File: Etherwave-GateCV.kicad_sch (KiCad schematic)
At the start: 57 parts, among them J1 Etherwave Brd, J2 Volume CV, J3 Pitch CV, J4 Gate, Q1 PMP4501Y, Q2 PMBT3906, Q3 PMP4501Y, U1 LM13700, U2 CD4093, U3 CD4093, U4 4022, U5 TL072, U6 4016, U7 TL072

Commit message: completed control circuit
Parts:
- added C12, C13: 100nF, symbol Device:C
- added D1: 1N4148, Diode_THT:D_DO-35_SOD27_P7.62mm_Horizontal, symbol Diode:1N4148
- added R27, R40: 330R, symbol Device:R
- added R28: 220k, symbol Device:R
- added R8, R9: 22k, symbol Device:R
- U4: value 4022 -> CD4022
- U6: value 4016 -> CD4016
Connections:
- net +12V: now also R8.2
- net GND: now also J3.1 (Pin_1), U1.13 (-), U6.2, U6.3, U7.3 (+), C12.2, C13.2, D1.2 (A), R9.1
- net at U5.5 (+): now also U6.10, U6.9, C13.1
- net at U5.6 (-): now also U5.7, R28.2
- net at U6.11: now also U6.8, R27.1
- net at U6.12: now also U4.3 (Q2), U6.6
- net at U7.2 (-): now also J3.3 (Pin_3), R28.1
- net at U6.4: now also U6.1, R40.1
- net at U6.5: now also U4.7 (Q3), U6.13
- net at Q2.3 (C): now also U1.16
- net at U5.1: now also U5.2 (-), D1.1 (K), R27.2
- net at U5.3 (+): now also U1.12, C12.1, R40.2
- net at U1.14 (+): now also R8.1, R9.2
- no-connect marks 11 -> 12
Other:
- note added: "FILM"
- moved on the sheet: D?, J2, J3, J4, Q3A, Q3B, U1A, U5A, U5B, U6A, U6B, U6C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

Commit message: circuit completed
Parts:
- removed D?: BAT54S, Package_TO_SOT_SMD:SOT-23, symbol Diode:BAT54S
- added C14: 330pF, symbol Device:C
- added C15: 100pF 50V, symbol Device:C
- added D2: 1N4148, Diode_THT:D_DO-35_SOD27_P7.62mm_Horizontal, symbol Diode:1N4148
- added D5: BAT54S, Package_TO_SOT_SMD:SOT-23, symbol Diode:BAT54S
- added R29, R34: 330R, symbol Device:R
- added R30, R32: 47k, symbol Device:R
- added R31: 1M24, symbol Device:R
- added R33: 470k, symbol Device:R
- added RV1, RV2: 50k, symbol Device:R_Potentiometer
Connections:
- net +12V: now also D5.2, R31.1, RV2.3
- net -12V: now also RV2.1
- net GND: now also Q3.2 (B2), U7.5 (+), D5.1, R29.2
- net at Q3.3 (C2): now also R28.1, U7.2 (-), C14.1
- net at Q3.4 (E2): now also Q3.5 (E1), R30.1
- net at U7.1: now also RV1.1
- net at U7.6 (-): now also Q3.6 (C1), C15.1, D2.1 (K), R31.2
- net at U7.7: now also C15.2, D2.2 (A), R30.2
- net at Q3.1 (B1): now also R29.1, R32.2, R33.2
- new net: D5.3, J3.3 (Pin_3), R34.1
- new net: R33.1, RV2.2
- new net: C14.2, R34.2
- new net: R32.1, RV1.2, RV1.3
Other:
- note added: "3500 PPM PTC 1W 3%"
- note added: "5%"
- moved on the sheet: J3, R18, R19, U7A, U7B

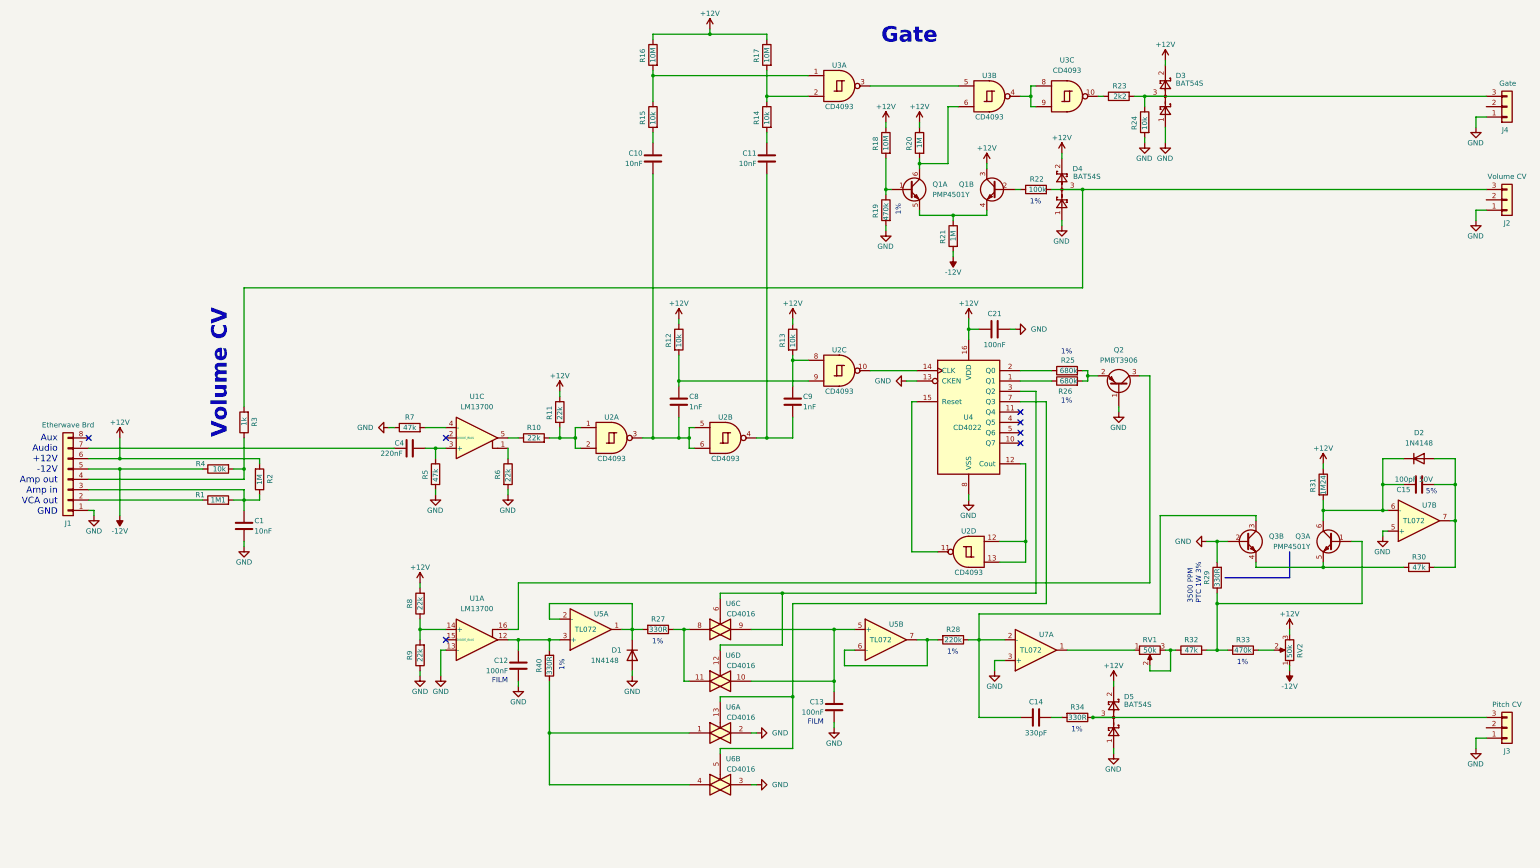
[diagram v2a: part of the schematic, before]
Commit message: completed footprint assignment
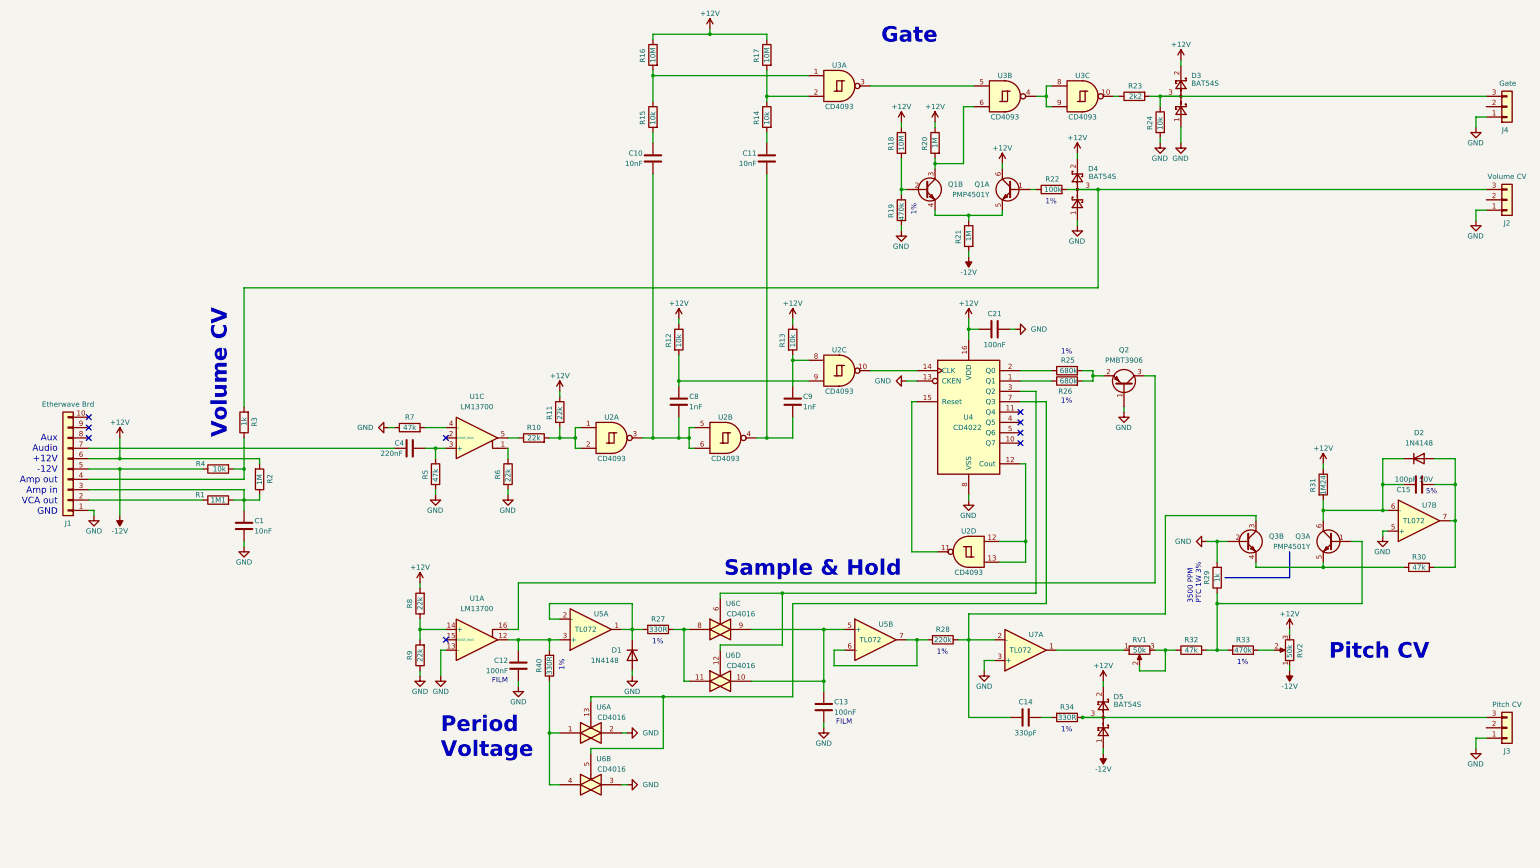
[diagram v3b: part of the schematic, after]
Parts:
- removed J1: Etherwave Brd, symbol Connector_Generic:Conn_01x08
- added J1: Etherwave Brd, Connector_Molex:Molex_KK-254_AE-6410-10A_1x10_P2.54mm_Vertical, symbol Connector_Generic:Conn_01x10
- C1, C10, C11, C12, C13, C14, C15, C16, C17, C18, C19, C20, C21, C22, C4, C5, C6, C7, C8, C9: footprint (none) -> Capacitor_SMD:C_0603_1608Metric_Pad1.08x0.95mm_HandSolder
- D1, D2: footprint Diode_THT:D_DO-35_SOD27_P7.62mm_Horizontal -> Diode_SMD:D_SOD-323_HandSoldering
- J2, J3, J4: footprint (none) -> Connector_Molex:Molex_KK-254_AE-6410-03A_1x03_P2.54mm_Vertical
- R1, R10, R11, R12, R13, R14, R15, R16, R17, R18, R19, R2, R20, R21, R22, R23, R24, R25, R26, R27, R28, R3, R30, R31, R32, R33, R34, R4, R40, R5, R6, R7, R8, R9: footprint (none) -> Resistor_SMD:R_0603_1608Metric_Pad0.98x0.95mm_HandSolder
- R29: value 330R -> 1k; footprint (none) -> Resistor_SMD:R_0603_1608Metric_Pad0.98x0.95mm_HandSolder
- RV1, RV2: footprint (none) -> Potentiometer_THT:Potentiometer_Bourns_3266Z_Horizontal
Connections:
- net +12V: now also Q1.6 (C1), J1.6 (Pin_6); no longer Q1.3 (C2)
- net -12V: now also D5.1, J1.5 (Pin_5)
- net GND: now also J1.1 (Pin_1); no longer D5.1
- net at R18.2, R19.1: now also Q1.2 (B2); no longer Q1.1 (B1)
- net at R1.1: now also J1.2 (Pin_2)
- net at C1.1, R1.2, R2.1: now also J1.3 (Pin_3)
- net at R3.1, R4.2: now also J1.4 (Pin_4)
- net at C4.1: now also J1.7 (Pin_7)
- net at R20.2, U3.6: now also Q1.3 (C2); no longer Q1.6 (C1)
- net at R22.1: now also Q1.1 (B1); no longer Q1.2 (B2)
- no-connect marks 12 -> 14
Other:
- note added: "Period Voltage"
- note added: "Pitch CV"
- note added: "Sample & Hold"
- moved on the sheet: C13, C14, D3, D4, D5, Q1A, Q1B, Q2, R18, R19, R20, R21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

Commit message: changed some special device footprint (C12, C13), created board file
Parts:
- C12, C13: footprint Capacitor_SMD:C_0603_1608Metric_Pad1.08x0.95mm_HandSolder -> Capacitor_SMD:C_1812_4532Metric_Pad1.57x3.40mm_HandSolder
- R29: value 1k -> 1k PTC
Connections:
- no-connect marks 14 -> 17
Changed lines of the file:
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@@
   (no_connect (at 266.7 125.73))
   (no_connect (at 266.7 120.65))
+  (no_connect (at 381 195.58))
   (no_connect (at 290.83 251.46))
   (no_connect (at 294.64 273.05))
   (no_connect (at 281.94 273.05))
+  (no_connect (at 381 43.18))
   (no_connect (at 271.78 270.51))
   (no_connect (at 38.1 119.38))
+  (no_connect (at 381 66.04))
   (no_connect (at 266.7 123.19))
   (no_connect (at 38.1 124.46))
@@
     (stroke (width 0) (type default) (color 0 0 0 0))
   )
-  (polyline (pts (xy 316.865 158.75) (xy 332.74 158.75))
+  (polyline (pts (xy 318.77 158.75) (xy 332.74 158.75))
     (stroke (width 0) (type default) (color 0 0 0 0))
   )
@@
       (effects (font (size 1.27 1.27)) (justify left))
     )
-    (property "Footprint" "Capacitor_SMD:C_0603_1608Metric_Pad1.08x0.95mm_HandSolder" (id 2) (at 219.4052 194.31 0)
+    (property "Footprint" "Capacitor_SMD:C_1812_4532Metric_Pad1.57x3.40mm_HandSolder" (id 2) (at 219.4052 194.31 0)
       (effects (font (size 1.27 1.27)) hide)
     )
@@
     (in_bom yes) (on_board yes)
     (property "Reference" "R29" (id 0) (at 312.42 158.75 90))
-    (property "Value" "1k" (id 1) (at 314.96 158.75 90))
+    (property "Value" "1k PTC" (id 1) (at 317.5 158.75 90))
     (property "Footprint" "Resistor_SMD:R_0603_1608Metric_Pad0.98x0.95mm_HandSolder" (id 2) (at 316.738 158.75 90)
       (effects (font (size 1.27 1.27)) hide)
@@
       (effects (font (size 1.27 1.27)) (justify left))
     )
-    (property "Footprint" "Capacitor_SMD:C_0603_1608Metric_Pad1.08x0.95mm_HandSolder" (id 2) (at 142.5448 184.15 0)
+    (property "Footprint" "Capacitor_SMD:C_1812_4532Metric_Pad1.57x3.40mm_HandSolder" (id 2) (at 142.5448 184.15 0)
       (effects (font (size 1.27 1.27)) hide)
     )
@@
     )
     (path "/e7a7453e-5366-4929-b035-bdefeb7eea3a"
-      (reference "C12") (unit 1) (value "100nF") (footprint "Capacitor_SMD:C_0603_1608Metric_Pad1.08x0.95mm_HandSolder")
+      (reference "C12") (unit 1) (value "100nF") (footprint "Capacitor_SMD:C_1812_4532Metric_Pad1.57x3.40mm_HandSolder")
     )
     (path "/06bab2f5-76a0-422d-a8c3-61f13004eda0"
-      (reference "C13") (unit 1) (value "100nF") (footprint "Capacitor_SMD:C_0603_1608Metric_Pad1.08x0.95mm_HandSolder")
+      (reference "C13") (unit 1) (value "100nF") (footprint "Capacitor_SMD:C_1812_4532Metric_Pad1.57x3.40mm_HandSolder")
     )
     (path "/70d7ccc4-e410-4031-9b58-7a1d91596003"
@@
     )
     (path "/bc92640f-f764-4894-8c59-db579eb0b508"
-      (reference "R29") (unit 1) (value "1k") (footprint "Resistor_SMD:R_0603_1608Metric_Pad0.98x0.95mm_HandSolder")
+      (reference "R29") (unit 1) (value "1k PTC") (footprint "Resistor_SMD:R_0603_1608Metric_Pad0.98x0.95mm_HandSolder")
     )
     (path "/ff9dbb00-bd33-48e4-aaac-7590c929ad89"

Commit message: about 40 % layout done
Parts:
- U5: footprint Package_SO:TSSOP-8_3x3mm_P0.65mm -> Package_SO:SOIC-8_3.9x4.9mm_P1.27mm
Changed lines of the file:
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@@
     (property "Reference" "U5" (id 0) (at 233.68 170.18 0))
     (property "Value" "TL072" (id 1) (at 229.87 173.99 0))
-    (property "Footprint" "Package_SO:TSSOP-8_3x3mm_P0.65mm" (id 2) (at 231.14 173.99 0)
+    (property "Footprint" "Package_SO:SOIC-8_3.9x4.9mm_P1.27mm" (id 2) (at 231.14 173.99 0)
       (effects (font (size 1.27 1.27)) hide)
     )
@@
       (effects (font (size 1.27 1.27)) (justify left))
     )
-    (property "Footprint" "Package_SO:TSSOP-8_3x3mm_P0.65mm" (id 2) (at 210.82 260.35 0)
+    (property "Footprint" "Package_SO:SOIC-8_3.9x4.9mm_P1.27mm" (id 2) (at 210.82 260.35 0)
       (effects (font (size 1.27 1.27)) hide)
     )
@@
     (property "Reference" "U5" (id 0) (at 163.83 167.64 0))
     (property "Value" "TL072" (id 1) (at 160.02 171.45 0))
-    (property "Footprint" "Package_SO:TSSOP-8_3x3mm_P0.65mm" (id 2) (at 161.29 171.45 0)
+    (property "Footprint" "Package_SO:SOIC-8_3.9x4.9mm_P1.27mm" (id 2) (at 161.29 171.45 0)
       (effects (font (size 1.27 1.27)) hide)
     )
@@
     )
     (path "/7bfba61b-6752-4a45-9ee6-5984dcb15041"
-      (reference "U5") (unit 1) (value "TL072") (footprint "Package_SO:TSSOP-8_3x3mm_P0.65mm")
+      (reference "U5") (unit 1) (value "TL072") (footprint "Package_SO:SOIC-8_3.9x4.9mm_P1.27mm")
     )
     (path "/07b7ccce-8895-49f2-b220-e85ac43040b1"
-      (reference "U5") (unit 2) (value "TL072") (footprint "Package_SO:TSSOP-8_3x3mm_P0.65mm")
+      (reference "U5") (unit 2) (value "TL072") (footprint "Package_SO:SOIC-8_3.9x4.9mm_P1.27mm")
     )
     (path "/2451d668-51ff-44ab-acfe-cfe666fa0c7e"
-      (reference "U5") (unit 3) (value "TL072") (footprint "Package_SO:TSSOP-8_3x3mm_P0.65mm")
+      (reference "U5") (unit 3) (value "TL072") (footprint "Package_SO:SOIC-8_3.9x4.9mm_P1.27mm")
     )
     (path "/537c74a2-24ab-4953-aadf-87353f9087ac"

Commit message: added mounting holes
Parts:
- added H1, H2, H3, H4: MountingHole, MountingHole:MountingHole_3.2mm_M3_DIN965, symbol Mechanical:MountingHole
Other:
- note added: "Mounting Holes M3"
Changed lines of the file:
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@@
     (effects (font (size 1.27 1.27)) (justify left bottom))
   )
+  (text "Mounting Holes M3" (at 105.41 261.62 180)
+    (effects (font (size 1.27 1.27)) (justify right bottom))
+  )
   (text "1%" (at 241.3 69.85 90)
     (effects (font (size 1.27 1.27)) (justify left bottom))
@@
     (pin "2")
   )
+  (symbol (lib_id "Mechanical:MountingHole") (at 101.6 254 0) (unit 1)
+    (in_bom yes) (on_board yes) (fields_autoplaced)
+    (property "Reference" "H2" (id 0) (at 104.14 253.9999 0)
+      (effects (font (size 1.27 1.27)) (justify left))
+    )
+    (property "Value" "MountingHole" (id 1) (at 104.14 255.2699 0)
+      (effects (font (size 1.27 1.27)) (justify left) hide)
+    )
+    (property "Footprint" "MountingHole:MountingHole_3.2mm_M3_DIN965" (id 2) (at 101.6 254 0)
+      (effects (font (size 1.27 1.27)) hide)
+    )
+    (property "Datasheet" "~" (id 3) (at 101.6 254 0)
+      (effects (font (size 1.27 1.27)) hide)
+    )
+  )
   (symbol (lib_id "Device:C") (at 204.47 55.88 0) (mirror y) (unit 1)
     (in_bom yes) (on_board yes)
@@
     (pin "6")
   )
+  (symbol (lib_id "Mechanical:MountingHole") (at 101.6 266.7 0) (unit 1)
+    (in_bom yes) (on_board yes) (fields_autoplaced)
+    (property "Reference" "H4" (id 0) (at 104.14 266.6999 0)
+      (effects (font (size 1.27 1.27)) (justify left))
+    )
+    (property "Value" "MountingHole" (id 1) (at 104.14 267.9699 0)
+      (effects (font (size 1.27 1.27)) (justify left) hide)
+    )
+    (property "Footprint" "MountingHole:MountingHole_3.2mm_M3_DIN965" (id 2) (at 101.6 266.7 0)
+      (effects (font (size 1.27 1.27)) hide)
+    )
+    (property "Datasheet" "~" (id 3) (at 101.6 266.7 0)
+      (effects (font (size 1.27 1.27)) hide)
+    )
+  )
   (symbol (lib_id "power:GND") (at 171.45 182.88 0) (unit 1)
     (in_bom yes) (on_board yes)
@@
     (pin "1")
   )
+  (symbol (lib_id "Mechanical:MountingHole") (at 88.9 254 0) (unit 1)
+    (in_bom yes) (on_board yes) (fields_autoplaced)
+    (property "Reference" "H1" (id 0) (at 91.44 253.9999 0)
+      (effects (font (size 1.27 1.27)) (justify left))
+    )
+    (property "Value" "MountingHole" (id 1) (at 91.44 255.2699 0)
+      (effects (font (size 1.27 1.27)) (justify left) hide)
+    )
+    (property "Footprint" "MountingHole:MountingHole_3.2mm_M3_DIN965" (id 2) (at 88.9 254 0)
+      (effects (font (size 1.27 1.27)) hide)
+    )
+    (property "Datasheet" "~" (id 3) (at 88.9 254 0)
+      (effects (font (size 1.27 1.27)) hide)
+    )
+  )
   (symbol (lib_id "Diode:1N4148") (at 364.49 129.54 0) (unit 1)
     (in_bom yes) (on_board yes) (fields_autoplaced)
@@
     (pin "1")
   )
+  (symbol (lib_id "Mechanical:MountingHole") (at 88.9 266.7 0) (unit 1)
+    (in_bom yes) (on_board yes) (fields_autoplaced)
+    (property "Reference" "H3" (id 0) (at 91.44 266.6999 0)
+      (effects (font (size 1.27 1.27)) (justify left))
+    )
+    (property "Value" "MountingHole" (id 1) (at 91.44 267.9699 0)
+      (effects (font (size 1.27 1.27)) (justify left) hide)
+    )
+    (property "Footprint" "MountingHole:MountingHole_3.2mm_M3_DIN965" (id 2) (at 88.9 266.7 0)
+      (effects (font (size 1.27 1.27)) hide)
+    )
+    (property "Datasheet" "~" (id 3) (at 88.9 266.7 0)
+      (effects (font (size 1.27 1.27)) hide)
+    )
+  )
   (symbol (lib_id "Device:R") (at 278.13 193.04 270) (unit 1)
     (in_bom yes) (on_board yes)
@@
       (reference "D5") (unit 1) (value "BAT54S") (footprint "Package_TO_SOT_SMD:SOT-23")
     )
+    (path "/e498b809-36c2-4aa1-ba30-c8056c032db3"
+      (reference "H1") (unit 1) (value "MountingHole") (footprint "MountingHole:MountingHole_3.2mm_M3_DIN965")
+    )
+    (path "/ab1a437f-5a70-434b-897c-748cd225449a"
+      (reference "H2") (unit 1) (value "MountingHole") (footprint "MountingHole:MountingHole_3.2mm_M3_DIN965")
+    )
+    (path "/ef047a17-9f04-4faa-b402-133d0186d6b8"
+      (reference "H3") (unit 1) (value "MountingHole") (footprint "MountingHole:MountingHole_3.2mm_M3_DIN965")
+    )
+    (path "/c22a6f6c-a527-478b-b541-dba6c20bc2a7"
+      (reference "H4") (unit 1) (value "MountingHole") (footprint "MountingHole:MountingHole_3.2mm_M3_DIN965")
+    )
     (path "/c5ae6c6c-85f0-48cb-8a5d-cbba911f8050"

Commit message: factory output, BOM, assembly
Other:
- company: (none) -> Riven Hexagon Electronics
- title: (none) -> Etherwave Gate & CV Extension
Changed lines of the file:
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@@
 (kicad_sch (version 20211123) (generator eeschema)
   (paper "A3")
+  (title_block
+    (title "Etherwave Gate & CV Extension")
+    (date "2023-05-18")
+    (rev "0")
+    (company "Riven Hexagon Electronics")
+  )
   (junction (at 153.67 124.46) (diameter 0) (color 0 0 0 0)
   )
